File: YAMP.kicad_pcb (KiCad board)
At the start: 2 copper layers, 88.1 x 42.9 mm, 7 parts, among them SW1 SW_Push, SW2 SW_Push, SW3 SW_Push, SW4 SW_Push, SW5 SW_Push, SW6 SW_Push, U1 XIAO-RP2040-DIP

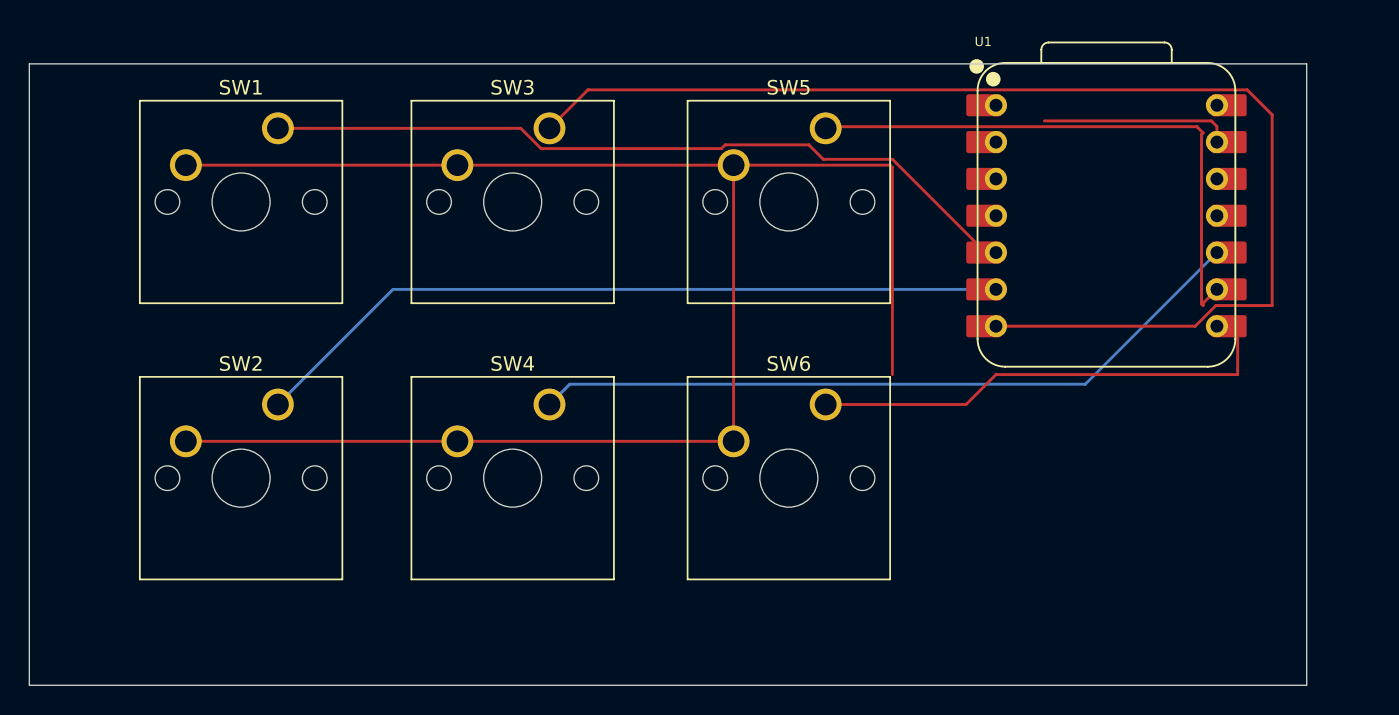
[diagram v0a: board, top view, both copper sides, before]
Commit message: add branding to PCB
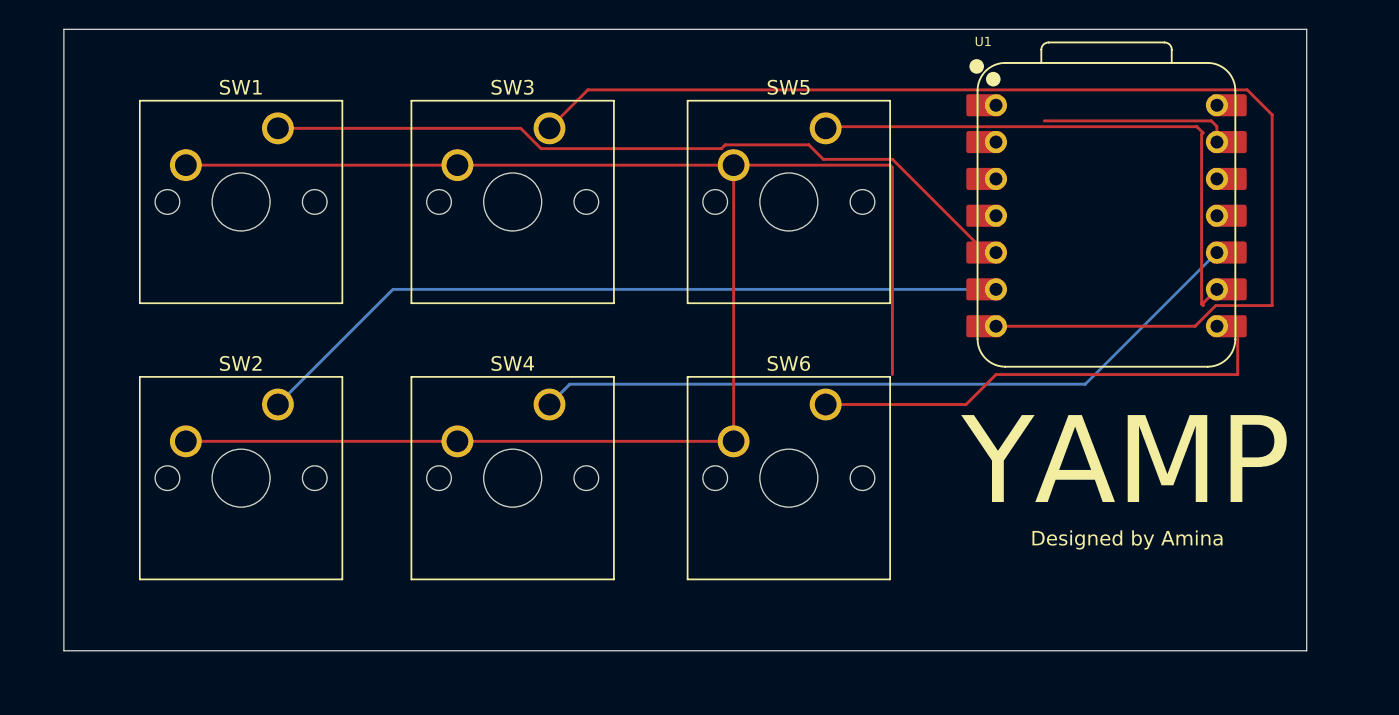
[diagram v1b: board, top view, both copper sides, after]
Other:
- board size 88.1 x 42.9 mm -> 85.7 x 42.9 mm
- board text added: "Designed by Amina"
- board text added: "YAMP"
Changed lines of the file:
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@@
 	)
 	(gr_rect
-		(start 50.00625 47.625)
-		(end 138.1125 90.4875)
+		(start 52.3875 45.24375)
+		(end 138.1125 88.10625)
 		(stroke
 			(width 0.05)
@@
 		(layer "Edge.Cuts")
 	)
+	(gr_text "Designed by Amina\n"
+		(at 119.0625 80.9625 0)
+		(layer "F.SilkS")
+		(effects
+			(font
+				(size 1 1)
+				(thickness 0.1)
+			)
+			(justify left bottom)
+		)
+	)
+	(gr_text "YAMP"
+		(at 114.3 78.58125 0)
+		(layer "F.SilkS")
+		(effects
+			(font
+				(size 6 6)
+				(thickness 0.1)
+			)
+			(justify left bottom)
+		)
+	)
 	(segment
